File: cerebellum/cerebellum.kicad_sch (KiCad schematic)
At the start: 59 parts

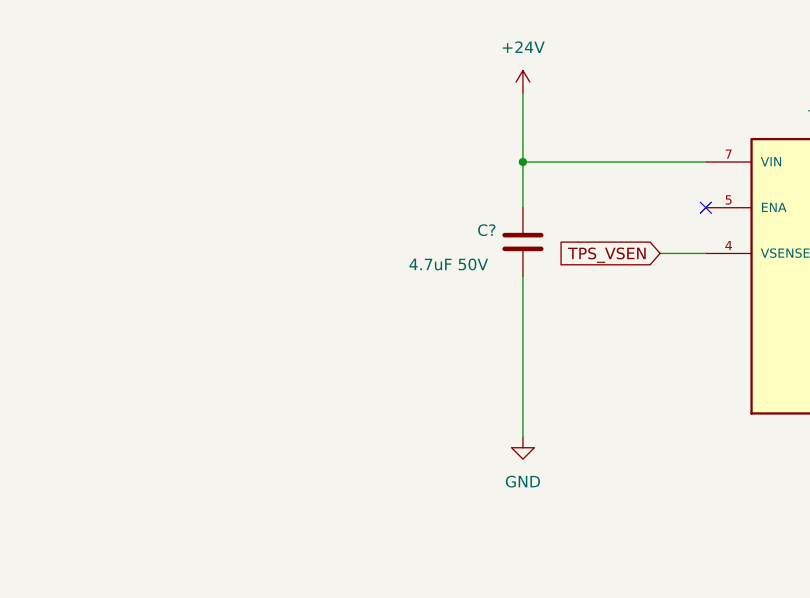
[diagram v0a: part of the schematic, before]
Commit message: [New] Add tvs to cerebellum
Signed-off-by: Homalozoa <nx.tardis@gmail.com>
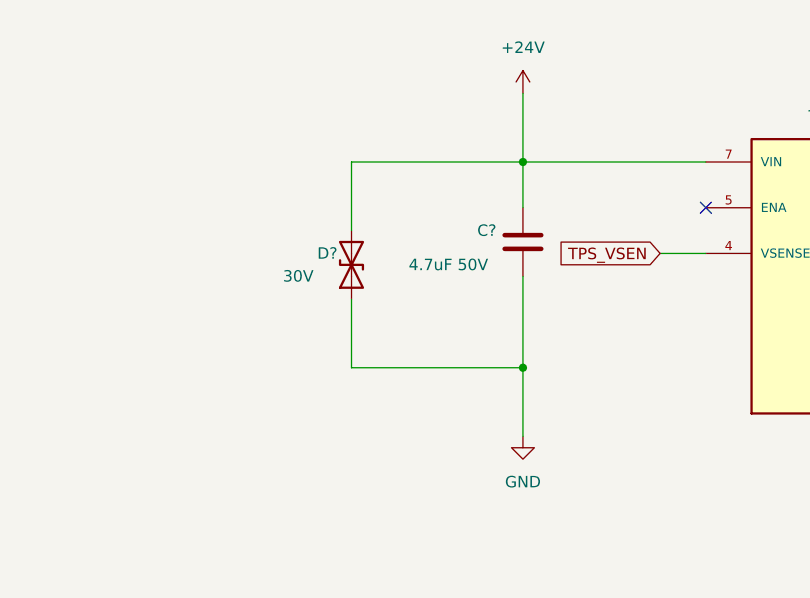
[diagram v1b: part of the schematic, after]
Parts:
- added D?: 30V, Diode_SMD:D_SMA, symbol Device:D_TVS
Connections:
- net +24V: now also D?.2 (A2)
- net GND: now also D?.1 (A1)
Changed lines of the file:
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@@
   (junction (at 185.42 207.01) (diameter 0) (color 0 0 0 0)
   )
+  (junction (at 370.84 86.36) (diameter 0) (color 0 0 0 0)
+  )
   (junction (at 487.68 322.58) (diameter 0) (color 0 0 0 0)
   )
@@
     (stroke (width 0) (type default) (color 0 0 0 0))
   )
+  (wire (pts (xy 370.84 63.5) (xy 370.84 68.58))
+    (stroke (width 0) (type default) (color 0 0 0 0))
+  )
   (wire (pts (xy 429.26 346.71) (xy 429.26 350.52))
     (stroke (width 0) (type default) (color 0 0 0 0))
@@
     (stroke (width 0) (type default) (color 0 0 0 0))
   )
+  (wire (pts (xy 370.84 63.5) (xy 351.79 63.5))
+    (stroke (width 0) (type default) (color 0 0 0 0))
+  )
   (wire (pts (xy 552.45 187.96) (xy 552.45 191.77))
     (stroke (width 0) (type default) (color 0 0 0 0))
@@
     (stroke (width 0) (type default) (color 0 0 0 0))
   )
-  (wire (pts (xy 495.3 322.58) (xy 495.3 325.12))
+  (wire (pts (xy 351.79 78.74) (xy 351.79 86.36))
     (stroke (width 0) (type default) (color 0 0 0 0))
   )
-  (wire (pts (xy 101.6 260.35) (xy 105.41 260.35))
+  (wire (pts (xy 495.3 322.58) (xy 495.3 325.12))
     (stroke (width 0) (type default) (color 0 0 0 0))
   )
-  (wire (pts (xy 370.84 63.5) (xy 370.84 68.58))
+  (wire (pts (xy 101.6 260.35) (xy 105.41 260.35))
     (stroke (width 0) (type default) (color 0 0 0 0))
   )
@@
     (stroke (width 0) (type default) (color 0 0 0 0))
   )
+  (wire (pts (xy 370.84 86.36) (xy 370.84 93.98))
+    (stroke (width 0) (type default) (color 0 0 0 0))
+  )
   (wire (pts (xy 429.26 334.01) (xy 429.26 339.09))
     (stroke (width 0) (type default) (color 0 0 0 0))
@@
     (stroke (width 0) (type default) (color 0 0 0 0))
   )
-  (wire (pts (xy 370.84 76.2) (xy 370.84 93.98))
+  (wire (pts (xy 370.84 76.2) (xy 370.84 86.36))
     (stroke (width 0) (type default) (color 0 0 0 0))
   )
@@
     (stroke (width 0) (type default) (color 0 0 0 0))
   )
+  (wire (pts (xy 351.79 86.36) (xy 370.84 86.36))
+    (stroke (width 0) (type default) (color 0 0 0 0))
+  )
   (wire (pts (xy 515.62 261.62) (xy 504.19 261.62))
     (stroke (width 0) (type default) (color 0 0 0 0))
@@
     (stroke (width 0) (type default) (color 0 0 0 0))
   )
+  (wire (pts (xy 351.79 63.5) (xy 351.79 71.12))
+    (stroke (width 0) (type default) (color 0 0 0 0))
+  )
   (wire (pts (xy 430.53 86.36) (xy 430.53 88.9))
     (stroke (width 0) (type default) (color 0 0 0 0))
@@
     (pin "2")
   )
+  (symbol (lib_id "Device:D_TVS") (at 351.79 74.93 90) (unit 1)
+    (in_bom yes) (on_board yes)
+    (property "Reference" "D?" (id 0) (at 347.98 73.66 90)
+      (effects (font (size 1.27 1.27)) (justify right))
+    )
+    (property "Value" "30V" (id 1) (at 344.17 76.2 90)
+      (effects (font (size 1.27 1.27)) (justify right))
+    )
+    (property "Footprint" "Diode_SMD:D_SMA" (id 2) (at 351.79 74.93 0)
+      (effects (font (size 1.27 1.27)) hide)
+    )
+    (property "Datasheet" "~" (id 3) (at 351.79 74.93 0)
+      (effects (font (size 1.27 1.27)) hide)
+    )
+    (pin "1")
+    (pin "2")
+  )
   (symbol (lib_id "Device:R_US") (at 533.4 184.15 0) (unit 1)
     (in_bom yes) (on_board yes)
@@
       (reference "C?") (unit 1) (value "4.7uF 50V") (footprint "Capacitor_SMD:C_0805_2012Metric")
     )
+    (path "/8875e8b5-e0bd-4a1d-a368-3553513f8fa7"
+      (reference "D?") (unit 1) (value "30V") (footprint "Diode_SMD:D_SMA")
+    )
     (path "/d6cf48a9-a13f-466f-bfde-8bc93913d1c0"

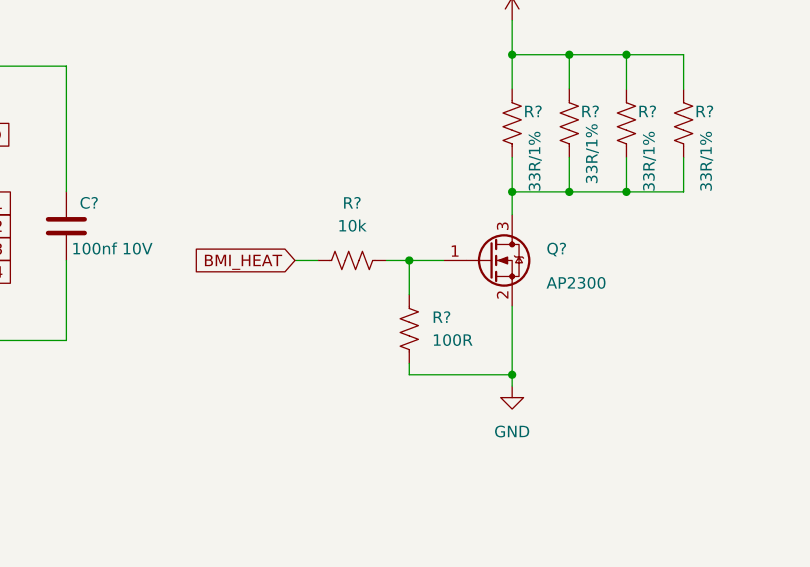
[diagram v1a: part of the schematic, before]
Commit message: [Fix] Exchange resistors in IMU heat circuit
Signed-off-by: Homalozoa X <nx.tardis@gmail.com>
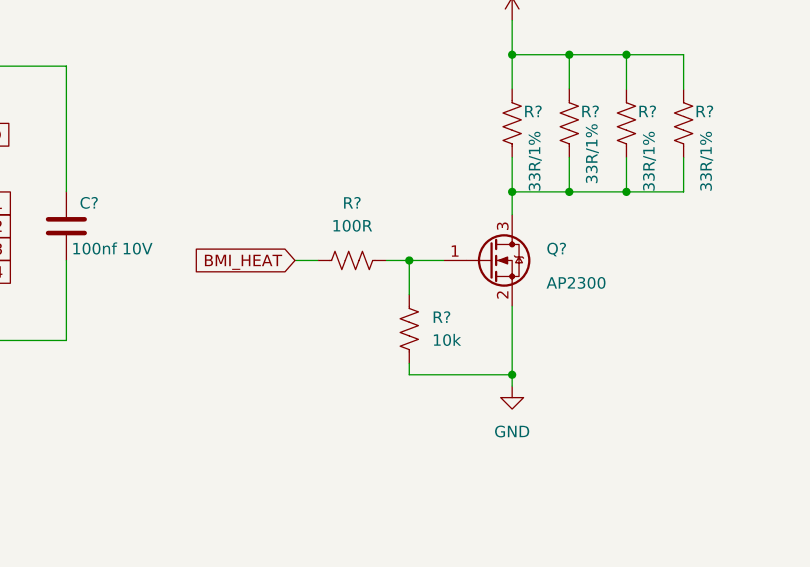
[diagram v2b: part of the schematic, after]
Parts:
- R?: value 10k -> 100R
- R?: value 100R -> 10k
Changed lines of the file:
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@@
     (in_bom yes) (on_board yes) (fields_autoplaced)
     (property "Reference" "R?" (id 0) (at 515.62 193.04 90))
-    (property "Value" "10k" (id 1) (at 515.62 195.58 90))
+    (property "Value" "100R" (id 1) (at 515.62 195.58 90))
     (property "Footprint" "Resistor_SMD:R_0402_1005Metric" (id 2) (at 515.366 200.406 90)
       (effects (font (size 1.27 1.27)) hide)
@@
       (effects (font (size 1.27 1.27)) (justify left))
     )
-    (property "Value" "100R" (id 1) (at 524.51 208.2799 0)
+    (property "Value" "10k" (id 1) (at 524.51 208.2799 0)
       (effects (font (size 1.27 1.27)) (justify left))
     )
@@
     )
     (path "/5cabeced-530f-4278-92c3-3ef338fb2515"
-      (reference "R?") (unit 1) (value "10k") (footprint "Resistor_SMD:R_0402_1005Metric")
+      (reference "R?") (unit 1) (value "100R") (footprint "Resistor_SMD:R_0402_1005Metric")
     )
     (path "/60ba2ac1-109e-441f-bbcc-6dcb6ced5367"
@@
     )
     (path "/a533392d-75e4-4fd1-9ce6-100ac3953ed1"
-      (reference "R?") (unit 1) (value "100R") (footprint "Resistor_SMD:R_0402_1005Metric")
+      (reference "R?") (unit 1) (value "10k") (footprint "Resistor_SMD:R_0402_1005Metric")
     )
     (path "/d719bbf9-5a30-418e-b968-c1f4d3570400"

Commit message: [Complete cerebellum schematic
* add gd32f405vghx to library

Signed-off-by: Homalozoa X <nx.tardis@gmail.com>
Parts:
- removed J?: XT30PW(2+2), Rolling_Custom:XT30PW(2+2), symbol Rolling_Custom:XT30PW(2+2)
- removed R?: 120R, Resistor_SMD:R_0402_1005Metric, symbol Device:R_US
- removed U?: GD32F405VGTx, Package_QFP:LQFP-100_14x14mm_P0.5mm, symbol Rolling_Custom:GD32F405VGTx
- added C29, C31: 4.7uF, 10%, 10V, Capacitor_SMD:C_0402_1005Metric, symbol Device:C
- added C30, C32: 100nF, 10%, 10V, Capacitor_SMD:C_0402_1005Metric, symbol Device:C
- added C? (x2): 10uF, 10%, 50V, Capacitor_SMD:C_0603_1608Metric, symbol Device:C
- added C?: 100nF, 10%, 50V, Capacitor_SMD:C_0402_1005Metric, symbol Device:C
- added C? (x2): 10pF, 10%, 50V, Capacitor_SMD:C_0402_1005Metric, symbol Device:C
- added C?: 10nF, 10%, 50V, Capacitor_SMD:C_0402_1005Metric, symbol Device:C
- added C?: 470nF, 10%, 50V, Capacitor_SMD:C_0603_1608Metric, symbol Device:C
- added C? (x2): 100pF, 10%, 10V, Capacitor_SMD:C_0402_1005Metric, symbol Device:C
- added J3: Conn_01x04, Connector_PinHeader_1.27mm:PinHeader_1x04_P1.27mm_Vertical, symbol Connector_Generic:Conn_01x04
- added J4: gh1.25, 3p, Connector_JST:JST_GH_SM03B-GHS-TB_1x03-1MP_P1.25mm_Horizontal, symbol Connector:Conn_01x03_Female
- added R?: 3k, Resistor_SMD:R_0402_1005Metric, symbol Device:R_US
- added R?: 33k, Resistor_SMD:R_0402_1005Metric, symbol Device:R_US
- added U1: GD32F405VGHx, Package_BGA:UFBGA-100_7x7mm_Layout12x12_P0.5mm, symbol Rolling_Custom:GD32F405VGHx
- added U?: TCAN4550RGYRQ1, Rolling_Custom:VQFN20, symbol Rolling_Custom:TCAN4550RGYRQ1
- added Y?: 40M, Oscillator:Oscillator_SMD_EuroQuartz_XO32-4Pin_3.2x2.5mm, symbol Device:Crystal_GND24
- D2: renamed from D?; footprint Diode_SMD:D_SMA -> Diode_SMD:D_SMC
- J1: renamed from J?; value XT30PW(2+2) -> PWR_OUT
- J2: renamed from J?; value XT30PW(2+2) -> PWR_IN
- gave numbers to parts that had none: 54
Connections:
- net +24V: now also C?.1, C?.1, R?.1, U?.14 (VSUP)
- net +3V3: now also C29.1, C30.1, C31.1, C32.1, J3.1 (Pin_1), U1.C4 (VDD), U1.E2 (VBAT), U1.G11 (VDD), U1.G12 (VDD), U1.G2 (VDD), U?.17 (VIO)
- net ACC_SCS: now also U1.A9 (PA15)
- net BMI_HEAT: now also U1.H10 (PD15)
- net BMI_INT1: now also U1.E10 (PC8)
- net BMI_INT2: now also U1.D10 (PA9)
- net BMI_INT3: now also U1.C8 (PD2)
- net BMI_INT4: now also U1.B7 (PD4)
- net BMI_SCK: now also U1.A8 (PB3)
- net BMI_SDI: now also U1.C5 (PB5)
- net BMI_SDO: now also U1.C10 (PC11)
- net CAN_H: now also C?.2, U?.11 (CANH)
- net CAN_L: now also C?.2, U?.10 (CANL)
- net GND: now also U2.10 (GND), U2.11 (GND), U2.12 (GND), U2.13 (GND), U2.14 (GND), U2.15 (GND), U2.16 (GND), U2.17 (GND), C29.2, C30.2, C31.2, C32.2, C?.1, C?.1, C?.1, C?.1, C?.1, C?.2, C?.2, C?.2, C?.2, J3.4 (Pin_4), J4.3 (Pin_3), U1.D3 (VSS), U1.F11 (VSS), U1.F12 (VSS), U1.F2 (VSS), U?.13 (GND), U?.21 (BTM), U?.22 (HOLE_22), U?.23 (HOLE_23), U?.24 (HOLE_24), U?.25 (HOLE_25), Y?.2, Y?.4
- net GYRO_SCS: now also U1.A12 (PA12)
- net ICP_INT: now also U1.K9 (PB11)
- net ICP_SCK: now also U1.K12 (PB13)
- net ICP_SDI: now also U1.K10 (PB15)
- net ICP_SDO: now also U1.J3 (PC2)
- net MCU_OSC_IN: now also U1.F1 (PH0)
- net MCU_OSC_OUT: now also U1.G1 (PH1)
- net NRST: now also U1.H2 (NRST)
- net TCAN_INT: now also U1.M5 (PB0)
- net TCAN_RST: now also U1.M6 (PB1)
- net TCAN_SCK: now also U1.K4 (PA5)
- net TCAN_SCS: now also U1.M3 (PA4)
- net TCAN_SDI: now also U1.M4 (PA7)
- net TCAN_SDO: now also U1.A7 (PB4)
- net TCAN_WKRQ: now also U1.M7 (PE7)
- net VREF_D: now also U1.M1 (VDDA)
- net VREF_S: now also U1.J1 (VSSA)
- net at R2.1: now also U1.A4 (BOOT0)
- net ISP_SCS renamed ICP_SCS
- net ICP_SCS: now also U1.L12 (PB12)
- new net: C?.2, R?.2, R?.2
- new net: C?.1, U?.18 (FLTR)
- new net Pi_VCCOUT: C?.1, U?.16 (VCCOUT)
- new net SWCLK: J3.3 (Pin_3), J4.2 (Pin_2), U1.A10 (PA14)
- new net SWDIO: J3.2 (Pin_2), J4.1 (Pin_1), U1.A11 (PA13)
- new net TCANPi_INT: U?.8 (~{INT})
- new net TCANPi_OSC_IN: C?.2, U?.1 (OSC1), Y?.1
- new net TCANPi_OSC_OUT: C?.2, U?.20 (OSC2), Y?.3
- new net TCANPi_RST: U?.19 (RST)
- new net TCANPi_SCK: U?.4 (SCLK)
- new net TCANPi_SCS: U?.7 (~{CS})
- new net TCANPi_SDI: U?.5 (SDI)
- new net TCANPi_SDO: U?.6 (SDO)
- new net TCANPi_WAKE: R?.1, U?.12 (WAKE)
- new net TCANPi_WKRQ: U?.2 (~{WKRQ})
- no-connect marks 4 -> 65
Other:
- note added: "Connectors"
- moved on the sheet: C1, C10, C11, C12, C13, C14, C15, C16, C17, C18, C19, C2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

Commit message: [New] Add cm4 to cerebellum
Signed-off-by: Homalozoa X <nx.tardis@gmail.com>
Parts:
- added C42, C43: 4.7uF 50V, Capacitor_SMD:C_0805_2012Metric, symbol Device:C
- added C44: 10uf 50V, Capacitor_SMD:C_0402_1005Metric, symbol Device:C
- added C45: 1.5nf 50V, Capacitor_SMD:C_0603_1608Metric, symbol Device:C
- added C46: 8.2nf 50V, Capacitor_SMD:C_0603_1608Metric, symbol Device:C
- added C47: 10pf 50V, Capacitor_SMD:C_0402_1005Metric, symbol Device:C
- added C48, C51: 100nF, 10%, 10V, Capacitor_SMD:C_0402_1005Metric, symbol Device:C
- added C49, C50: 47uf 50V, Capacitor_SMD:C_0603_1608Metric, symbol Device:C
- added D5: B240, Diode_SMD:D_SMB, symbol Diode:B240
- added J5: CM4_A, Rolling_Custom:HRS_DF40C-100DS-0.4V(51), symbol Rolling_Custom:DF40C-100DS-0.4V(51)
- added J6: CM4_B, Rolling_Custom:HRS_DF40C-100DS-0.4V(51), symbol Rolling_Custom:DF40C-100DS-0.4V(51)
- added J7: RJ45, Connector_RJ:RJ45_Molex_0855135013_Vertical, symbol Connector:RJ45
- added L3: 15uh, Inductor_SMD:L_0603_1608Metric, symbol Device:L
- added R17: 169k, Resistor_SMD:R_0402_1005Metric, symbol Device:R_US
- added R18: 20.5, Resistor_SMD:R_0402_1005Metric, symbol Device:R_US
- added R19: 64.9k, Resistor_SMD:R_0402_1005Metric, symbol Device:R_US
- added R20: 10.2k, Resistor_SMD:R_0402_1005Metric, symbol Device:R_US
- added R21: 1.96k, Resistor_SMD:R_0402_1005Metric, symbol Device:R_US
- added U6: TPS54231, Package_SO:SOIC-8_3.9x4.9mm_P1.27mm, symbol Regulator_Switching:TPS54233
- gave numbers to parts that had none: 13
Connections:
- net +24V: now also C42.1, C43.1, C44.1, R17.1, U6.2 (VIN)
- net +3V3: now also C51.1
- net GND: now also C42.2, C43.2, C44.2, C45.2, C46.2, C47.2, C49.2, C50.2, C51.2, D5.2 (A), J5.1, J5.13, J5.14, J5.2, J5.22, J5.23, J5.32, J5.33, J5.42, J5.43, J5.52, J5.53, J5.59, J5.60, J5.65, J5.66, J5.7, J5.71, J5.74, J5.8, J5.98, J6.13, J6.14, J6.19, J6.20, J6.25, J6.26, J6.31, J6.32, J6.37, J6.38, J6.44, J6.50, J6.55, J6.56, J6.61, J6.62, J6.67, J6.68, J6.7, J6.73, J6.74, J6.79, J6.8, J6.80, J6.85, J6.86, J6.91, J6.92, J6.97, J6.98, R18.2, R21.2, U6.7 (GND)
- new net: C48.2, U6.1 (BOOT)
- new net: R17.2, R18.1, U6.3 (EN)
- new net: C46.1, U6.4 (SS)
- new net: C48.1, L3.2, U6.8 (PH)
- new net: C45.1, R19.2
- new net +5V: C49.1, C50.1, D5.1 (K), J5.77, J5.79, J5.81, J5.83, J5.85, J5.87, L3.1, R20.1
- new net 5V_CMP: C47.1, R19.1, U6.6 (COMP)
- new net 5V_FB: R20.2, R21.1, U6.5 (FB)
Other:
- moved on the sheet: C1, C10, C11, C12, C13, C14, C15, C16, C17, C18, C19, C2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

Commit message: [New] NC serveral pins of CM4 & Add uPD720201
Signed-off-by: Homalozoa X <nx.tardis@gmail.com>
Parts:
- added R? (x2): 47k, Resistor_SMD:R_0402_1005Metric, symbol Device:R_US
- added U?: UPD720201K8-701-BAC-A, Rolling_Custom:QFN40P800X800X90-69N, symbol Rolling_Custom:UPD720201K8-701-BAC-A
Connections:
- net GND: now also R?.1, R?.1
- net TCANPi_SCK: now also J5.38
- net TCANPi_SCS: now also J5.39
- net TCANPi_SDI: now also J5.44
- net TCANPi_SDO: now also J5.40
- net USB_OTG_ID: now reaches J6.1
- net PCIe_CLK_nREQ: now reaches J6.2
- net USB_N: now reaches J6.3
- net USB_P: now reaches J6.5
- net Eth_0N: now reaches J5.10
- net CM4_nRST: now reaches J5.100
- net Eth_2P: now reaches J5.11
- net Eth_0P: now reaches J5.12
- net Eth_nLED3: now reaches J5.15
- net Eth_SyncIn: now reaches J5.16
- net Eth_nLED2: now reaches J5.17
- net Eth_SyncOut: now reaches J5.18
- net Eth_nLED1: now reaches J5.19
- net EEPROM_nWP: now reaches J5.20
- net nLED_Active: now reaches J5.21
- net Eth_3P: now reaches J5.3
- net Eth_1P: now reaches J5.4
- net Eth_3N: now reaches J5.5
- net Eth_1N: now reaches J5.6
- net CM4_3.3V: now reaches J5.78
- net CM4_3.3V: now also J5.84, J5.86
- net CM4_1.8V: now reaches J5.88
- net CM4_1.8V: now also J5.90
- net at J5.89: now also R?.2
- net Eth_2N: now reaches J5.9
- net at J5.91: now also R?.2
- net RUN_PG: now reaches J5.92
- net AnalogIP1: now reaches J5.94
- net PI_LED: now reaches J5.95
- net AnalogIP0: now reaches J5.96
- net CM4_EN: now reaches J5.99
- new net: U?.12 (VDD10), U?.28 (VDD10), U?.37 (VDD10), U?.43 (VDD10), U?.46 (VDD10), U?.54 (VDD10), U?.60 (VDD10), U?.63 (VDD10), U?.9 (VDD10)
- new net: U?.15 (VDD33), U?.29 (VDD33), U?.40 (VDD33), U?.49 (VDD33), U?.57 (VDD33), U?.66 (VDD33)
- new net: U?.32 (AVDD33), U?.6 (AVDD33)
- no-connect marks 65 -> 165
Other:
- moved on the sheet: C45, C47, J5, J6, R19, R2, U1

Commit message: [New] Add 1.05 LDO to cerebellum
Signed-off-by: Homalozoa <nx.tardis@gmail.com>
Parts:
- added C? (x2): 10pF, 10%, 50V, Capacitor_SMD:C_0402_1005Metric, symbol Device:C
- added C?: 1uF, 10%, 10V, Capacitor_SMD:C_0402_1005Metric, symbol Device:C
- added C? (x3): (no value), Capacitor_SMD:C_0402_1005Metric, symbol Device:C
- added C?: 100nF, 10%, 10V, Capacitor_SMD:C_0402_1005Metric, symbol Device:C
- added C?: 4.7uF, 10%, 10V, Capacitor_SMD:C_0402_1005Metric, symbol Device:C
- added C?: 10uF, 10%, 10V, Capacitor_SMD:C_0402_1005Metric, symbol Device:C
- added L?: (no value), Resistor_SMD:R_0402_1005Metric, symbol Device:L_Ferrite
- added R? (x2): (no value), Resistor_SMD:R_0402_1005Metric, symbol Device:R_US
- added U?: (no value), symbol Regulator_Linear:AP2127K-ADJ
- added Y?: (no value), Oscillator:Oscillator_SMD_EuroQuartz_XO32-4Pin_3.2x2.5mm, symbol Device:Crystal_GND24
- C14, C15, C33, C34: value 10pF, 10%, 50V -> (none)
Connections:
- net +3V3: now also U?.15 (VDD33), U?.29 (VDD33), U?.40 (VDD33), U?.49 (VDD33), U?.57 (VDD33), U?.66 (VDD33), C?.1, C?.1, C?.1, C?.1, L?.1
- net +5V: now also C?.1, U?.1 (VIN), U?.3 (EN)
- net GND: now also U?.69 (GND), C?.1, C?.1, C?.2, C?.2, C?.2, C?.2, C?.2, C?.2, R?.2, U?.2 (GND)
- net PCIe_CLK_N: now also J6.12, U?.5 (PECLKN)
- net PCIe_CLK_P: now also J6.10, U?.4 (PECLKP)
- net PCIe_CLK_nREQ: now also U?.13 (~{PECREQB})
- net PCIe_RX_N: now also J6.18, U?.11 (PERXN)
- net PCIe_RX_P: now also J6.16, U?.10 (PERXP)
- net PCIe_TX_N: now also J6.24, U?.8 (PETXN)
- net PCIe_TX_P: now also J6.22, U?.7 (PETXP)
- net PCIe_nRST: now also J6.9, U?.2 (~{PERSTB})
- net +1V0: now reaches U?.12 (VDD10), U?.28 (VDD10), U?.37 (VDD10), U?.43 (VDD10), U?.46 (VDD10), U?.54 (VDD10), U?.60 (VDD10), U?.63 (VDD10), U?.9 (VDD10)
- net +1V0: now also C?.1, C?.1, R?.1, U?.5 (VOUT)
- net UPD_OSC_OUT: now reaches U?.30 (XT2)
- net UPD_OSC_OUT: now also C?.2, Y?.3
- net UPD_OSC_IN: now reaches U?.31 (XT1)
- net UPD_OSC_IN: now also C?.2, Y?.1
- net at U?.32 (AVDD33), U?.6 (AVDD33): now also L?.2
- new net: C?.2, R?.1, R?.2, U?.4 (ADJ)

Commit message: [New] Add USB switches & flash to cerebellum
Signed-off-by: Homalozoa <nx.tardis@gmail.com>
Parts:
- added C? (x9): 100nF, 10%, 10V, Capacitor_SMD:C_0402_1005Metric, symbol Device:C
- added C? (x12): 47uf 50V, Capacitor_SMD:C_0603_1608Metric, symbol Device:C
- added C?: 1uF, 10%, 10V, Capacitor_SMD:C_0402_1005Metric, symbol Device:C
- added C? (x2): (no value), symbol Device:C
- added C?: 10uF, 10%, 10V, Capacitor_SMD:C_0402_1005Metric, symbol Device:C
- added R? (x3): 100k, Resistor_SMD:R_0402_1005Metric, symbol Device:R_US
- added R?: (no value), Resistor_SMD:R_0402_1005Metric, symbol Device:R_US
- added R? (x2): 4.7k, Resistor_SMD:R_0402_1005Metric, symbol Device:R_US
- added U? (x3): APL3553, Package_TO_SOT_SMD:SOT-23-5, symbol Rolling_Custom:APL3553
- added U?: (no value), symbol Rolling_Custom:APL3553
- added U?: (no value), Package_SON:USON-10_2.5x1.0mm_P0.5mm, symbol Power_Protection:TPD4EUSB30
- added U?: (no value), symbol Rolling_Custom:GD25Q40C
- added U?: TPD4EUSB30, Package_SON:USON-10_2.5x1.0mm_P0.5mm, symbol Power_Protection:TPD4EUSB30
- C14, C15, C33, C34: value (none) -> 8.2pF, 10%, 50V
- C? (x2): value 10pF, 10%, 50V -> (none)
- C?: value (none) -> 3nF, 10V
- C?: value (none) -> 10uF, 10%, 10V
- C?: value (none) -> 1uF, 10%, 10V
- L?: value (none) -> 0R
- R?: value (none) -> 4.7k
- R?: value (none) -> 15k
- U?: value (none) -> AP2127K-ADJ; footprint (none) -> Package_TO_SOT_SMD:SOT-23-5
- Y?: value (none) -> 24M
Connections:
- net +3V3: now also C?.1, C?.1, C?.1, R?.1, R?.1, U?.8 (VCC)
- net +5V: now also C?.1, C?.1, C?.1, C?.1, R?.2, R?.2, R?.2, R?.2, U?.5 (VIN), U?.5 (VIN), U?.5 (VIN), U?.5 (VIN)
- net Eth_0N: now also J7.2, U?.2 (D1-)
- net Eth_0P: now also J7.1, U?.1 (D1+)
- net Eth_1N: now also J7.4, U?.5 (D2-)
- net Eth_1P: now also J7.3, U?.4 (D2+)
- net Eth_2N: now also J7.6, U?.2 (D1-)
- net Eth_2P: now also J7.5, U?.1 (D1+)
- net Eth_3N: now also J7.8, U?.5 (D2-)
- net Eth_3P: now also J7.7, U?.4 (D2+)
- net GND: now also U?.34 (IC(L)), C?.2, C?.2, C?.2, C?.2, C?.2, C?.2, C?.2, C?.2, C?.2, C?.2, C?.2, C?.2, C?.2, C?.2, C?.2, C?.2, C?.2, C?.2, C?.2, C?.2, C?.2, C?.2, C?.2, U?.2 (GND), U?.2 (GND), U?.2 (GND), U?.2 (GND), U?.3 (GND), U?.3 (GND), U?.4 (VSS), U?.8 (GND), U?.8 (GND)
- net PCIe_RX_N: now also C?.1; no longer U?.11 (PERXN)
- net PCIe_RX_P: now also C?.1; no longer U?.10 (PERXP)
- net ROM_SDO: now reaches U?.16 (SPISO)
- net ROM_SDO: now also U?.2 (SO/IO1)
- net ROM_CS: now reaches U?.17 (SPICSB)
- net ROM_CS: now also U?.1 (CS)
- net ROM_SCK: now reaches U?.18 (SPISCK)
- net ROM_SCK: now also U?.6 (SCLK)
- net ROM_SDI: now reaches U?.19 (SPISI)
- net ROM_SDI: now also U?.5 (SI/IO0)
- net USB4_OCI: now reaches U?.20 (~{OCI4B})
- net USB4_OCI: now also U?.3 (OCB)
- net USB4_PON: now reaches U?.21 (PPON4)
- net USB4_PON: now also R?.1, U?.4 (EN/ENB)
- net USB3_OCI: now reaches U?.22 (~{OCI3B})
- net USB3_OCI: now also U?.3 (OCB)
- net USB3_PON: now reaches U?.23 (PPON3)
- net USB3_PON: now also R?.1, U?.4 (EN/ENB)
- net USB2_OCI: now reaches U?.24 (~{OCI2B})
- net USB2_OCI: now also U?.3 (OCB)
- net USB2_PON: now reaches U?.25 (PPON2)
- net USB2_PON: now also R?.1, U?.4 (EN/ENB)
- net USB1_OCI: now reaches U?.26 (~{OCI1B})
- net USB1_OCI: now also U?.3 (OCB)
- net USB1_PON: now reaches U?.27 (PPON1)
- net USB1_PON: now also R?.1, U?.4 (EN/ENB)
- new net: C?.2, U?.11 (PERXN)
- new net: C?.2, U?.10 (PERXP)
- new net: R?.2, U?.7 (HOLD/IO3)
- new net: R?.2, U?.3 (WP/IO2)
- new net VBUS1: C?.1, C?.1, C?.1, C?.1, U?.1 (VOUT)
- new net VBUS2: C?.1, C?.1, C?.1, C?.1, U?.1 (VOUT)
- new net VBUS3: C?.1, C?.1, C?.1, C?.1, U?.1 (VOUT)
- new net VBUS4: C?.1, C?.1, C?.1, C?.1, U?.1 (VOUT)
- no-connect marks 165 -> 166
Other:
- moved on the sheet: C1, C10, C11, C12, C13, C14, C15, C16, C17, C18, C19, C2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
